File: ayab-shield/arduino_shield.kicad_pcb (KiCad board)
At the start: 2 copper layers, 73.1 x 53.3 mm, 35 parts, among them IC1 ULN2803A, IC2 ULN2803A, IC3 MCP2300X/P, IC4 MCP2300X/P, J1 Power, J2 Digital/PWM, J3 Analog, J4 Digital/PWM, X1 KLDX-0202-AC

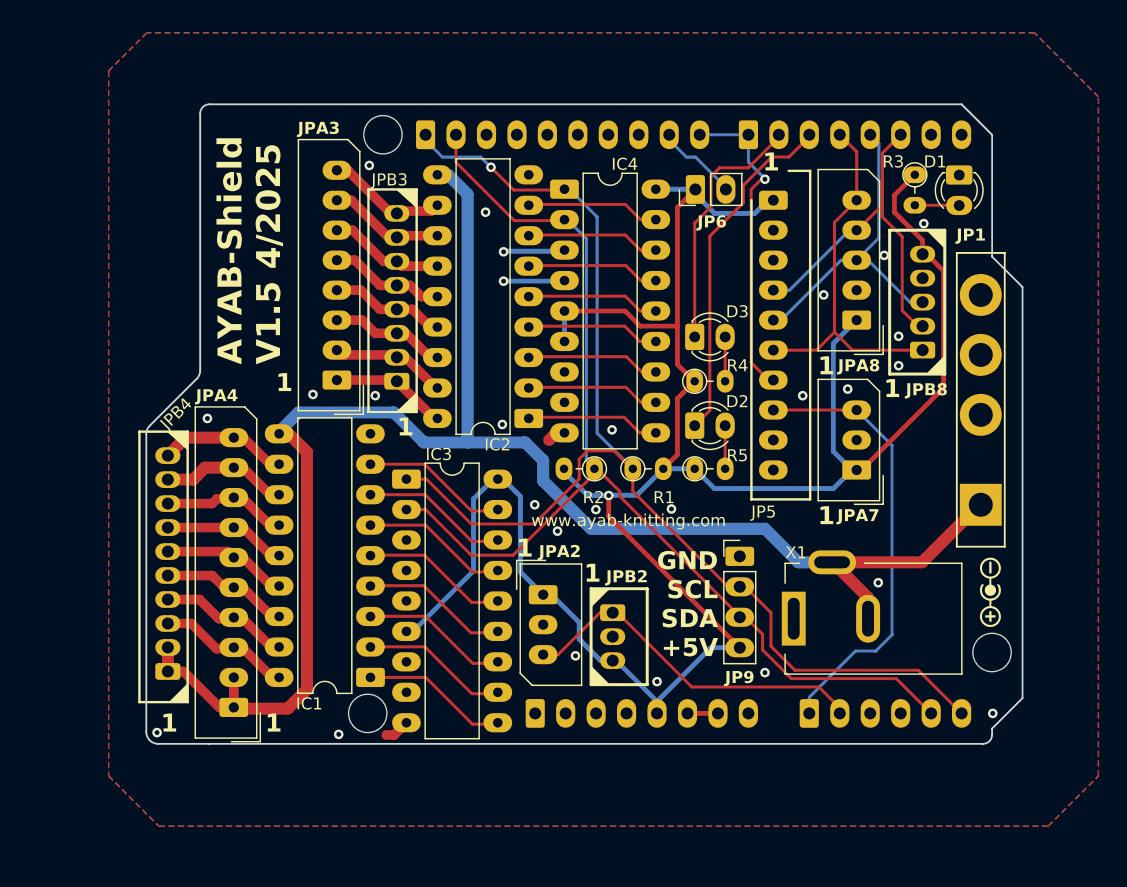
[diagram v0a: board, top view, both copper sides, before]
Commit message: Change footprints used on PCB to new footprints with '_LongPads' suffix
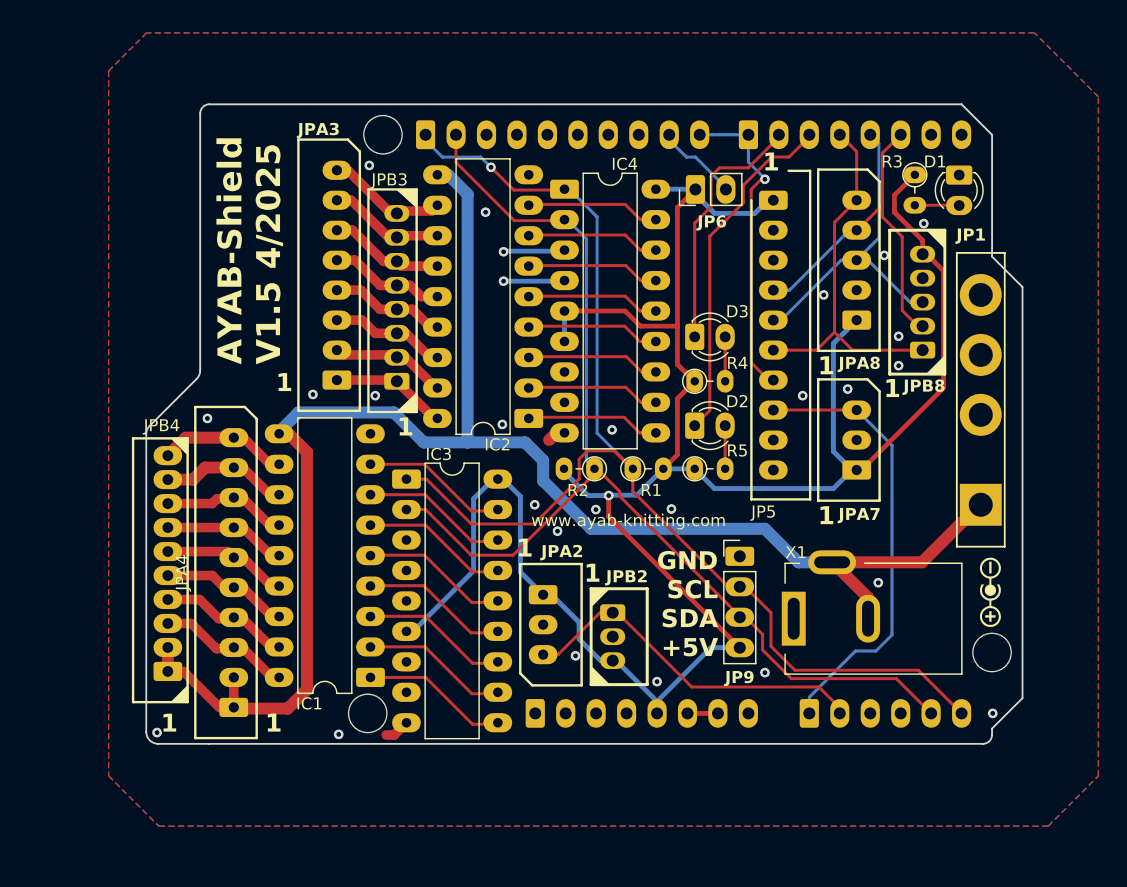
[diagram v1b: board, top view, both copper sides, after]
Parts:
- G***: value LOGO -> Polarity_Center_Negative_2mm_SilkScreen; footprint LOGO -> ayab-library:Polarity_Center_Negative_2mm_SilkScreen
- J2: footprint ayab-library:PinHeader_1x10_P2.54mm_Vertical -> ayab-library:PinHeader_1x10_P2.54mm_Vertical_LongPads
- JP5: footprint ayab-library:SHDR10W70P0X250_1X10_2740X490X590P -> ayab-library:SHDR10W70P0X250_1X10_2740X490X590P_LongPads
- JP6: footprint ayab-library:PinHeader_1x02_P2.54mm_Vertical -> ayab-library:PinHeader_1x02_P2.54mm_Vertical_LongPads
- JP9: footprint ayab-library:PinHeader_1x04_P2.54mm_Vertical -> ayab-library:PinHeader_1x04_P2.54mm_Vertical_LongPads
- JPA2, JPA7: footprint ayab-library:Molex_SPOX_5267-03A_1x03_P2.50mm_Vertical -> ayab-library:Molex_SPOX_5267-03A_1x03_P2.50mm_Vertical_LongPads
- JPA3: footprint ayab-library:Molex_SPOX_5267-08A_1x08_P2.50mm_Vertical -> ayab-library:Molex_SPOX_5267-08A_1x08_P2.50mm_Vertical_LongPads
- JPA4: footprint ayab-library:Molex_SPOX_5267-10A_1x10_P2.50mm_Vertical -> ayab-library:Molex_SPOX_5267-10A_1x10_P2.50mm_Vertical_LongPads
- JPA8: footprint ayab-library:Molex_SPOX_5267-05A_1x05_P2.50mm_Vertical -> ayab-library:Molex_SPOX_5267-05A_1x05_P2.50mm_Vertical_LongPads
- JPB4: footprint ayab-library:530141010 -> ayab-library:530141010_LongPads
- JPB8: footprint ayab-library:CONN-TH_A2004WV-5P -> ayab-library:CONN-TH_A2004WV-5P_LongPads
- R1, R2, R3, R4, R5: footprint ayab-library:R_Axial_DIN0204_L3.6mm_D1.6mm_P2.54mm_Vertical -> ayab-library:R_Axial_DIN0204_L3.6mm_D1.6mm_P2.54mm_Vertical_LongPads
- turned MH1 to -90 degrees

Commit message: Clean up
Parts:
- J1, J4: footprint ayab-library:PinHeader_1x08_P2.54mm_Vertical -> ayab-library:PinHeader_1x08_P2.54mm_Vertical_LongPads
- J3: footprint ayab-library:PinHeader_1x06_P2.54mm_Vertical -> ayab-library:PinHeader_1x06_P2.54mm_Vertical_LongPads
- JPB2: footprint ayab-library:CONN-TH_3P-P2.00_A2004WV-3P -> ayab-library:530140310_LongPads
- JPB3: footprint ayab-library:530140810 -> ayab-library:530140810_LongPads
- JPB8: footprint ayab-library:CONN-TH_A2004WV-5P_LongPads -> ayab-library:530140510_LongPads
- moved JPB8 4.04 mm to (175.0, 97.2)
- moved JPB2 2.04 mm to (149.1, 119.1)
- moved JPA3 0.46 mm to (125.6, 99.7)

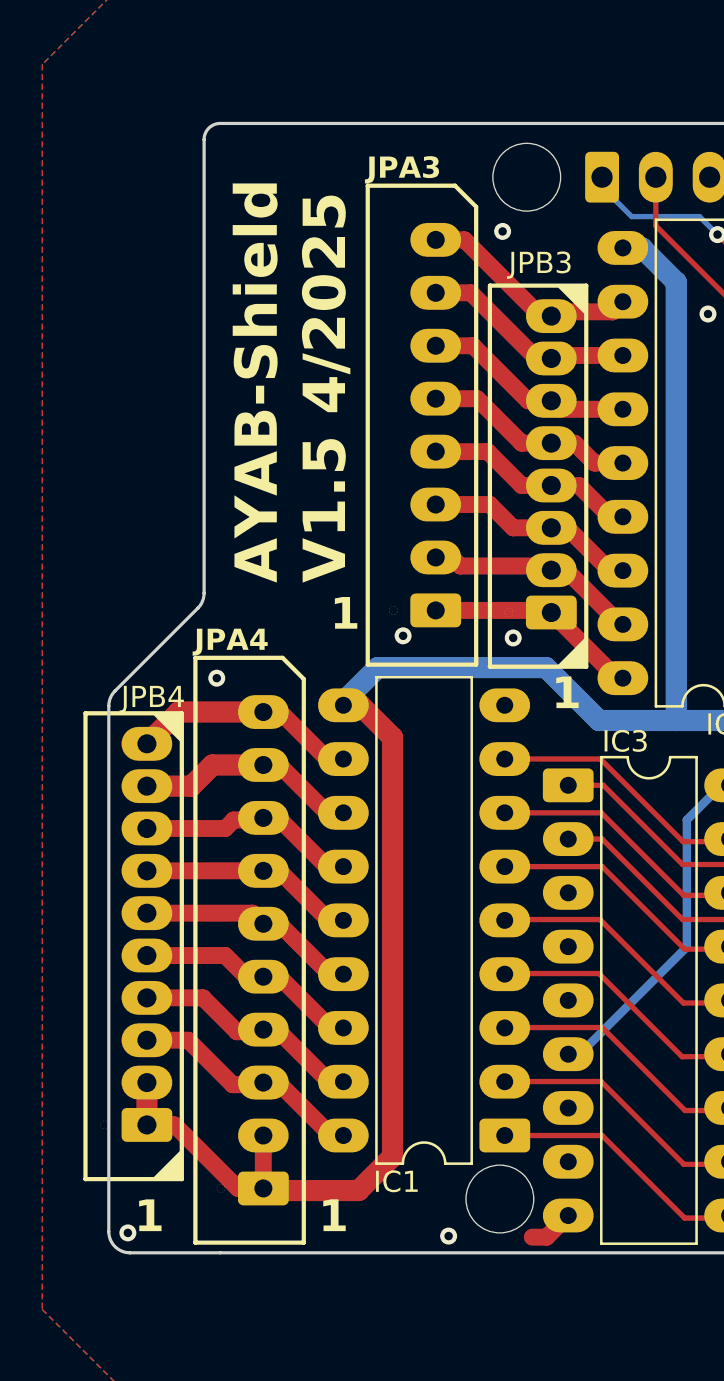
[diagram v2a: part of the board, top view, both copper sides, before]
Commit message: Reverse orientation of solenoid headers and extend PCB by 1mm
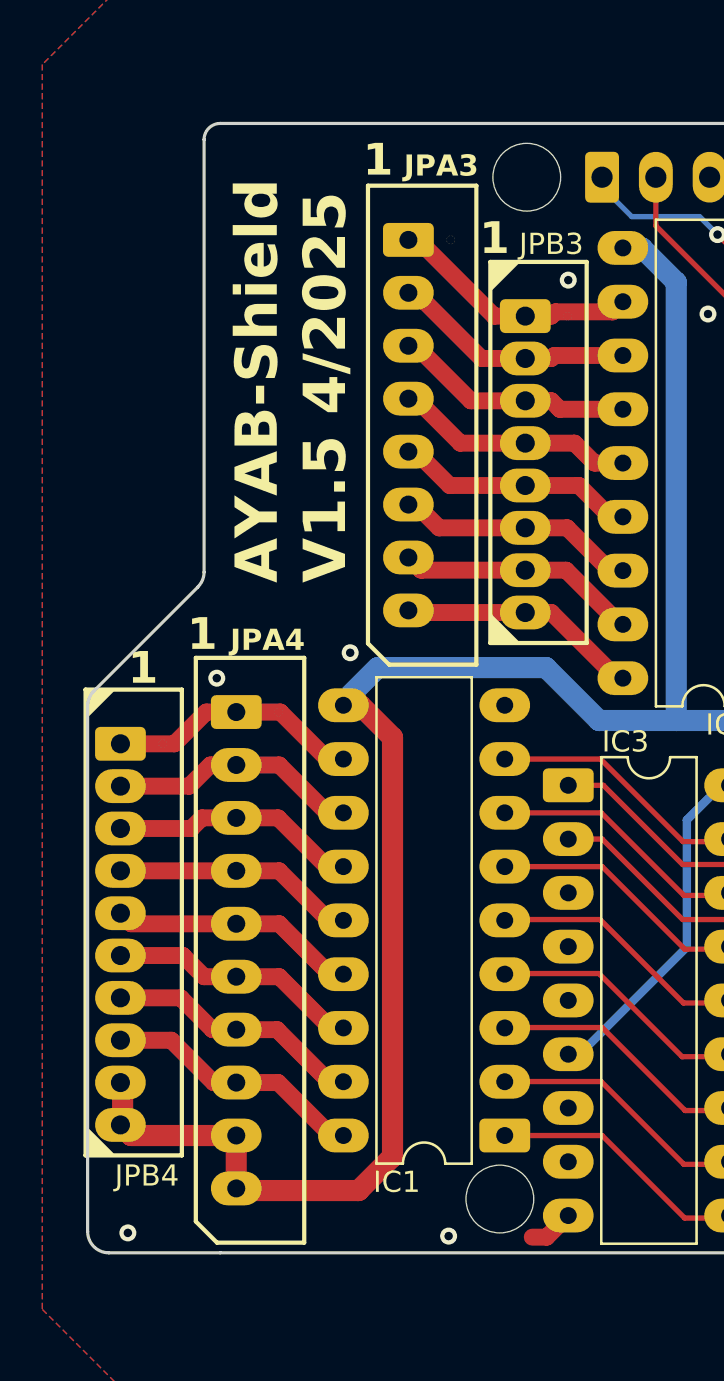
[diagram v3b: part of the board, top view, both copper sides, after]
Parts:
- moved JPA4 22.5 mm to (116.2, 104.5), turned to -90 degrees
- moved JPB4 18.0 mm to (110.8, 106.0), turned to 90 degrees
- moved JPA3 17.5 mm to (124.3, 82.2), turned to -90 degrees
- moved JPB3 14.1 mm to (129.9, 85.8), turned to 90 degrees
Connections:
- JPA3 pad 1: Net-(IC2-O1) -> Net-(IC2-O8)
- JPA3 pad 2: Net-(IC2-O2) -> Net-(IC2-O7)
- JPA3 pad 3: Net-(IC2-O3) -> Net-(IC2-O6)
- JPA3 pad 4: Net-(IC2-O4) -> Net-(IC2-O5)
- JPA3 pad 5: Net-(IC2-O5) -> Net-(IC2-O4)
- JPA3 pad 6: Net-(IC2-O6) -> Net-(IC2-O3)
- JPA3 pad 7: Net-(IC2-O7) -> Net-(IC2-O2)
- JPA3 pad 8: Net-(IC2-O8) -> Net-(IC2-O1)
- JPA4 pad 1: +15V -> Net-(IC1-O8)
- JPA4 pad 10: Net-(IC1-O8) -> +15V
- JPA4 pad 2: +15V -> Net-(IC1-O7)
- JPA4 pad 3: Net-(IC1-O1) -> Net-(IC1-O6)
- JPA4 pad 4: Net-(IC1-O2) -> Net-(IC1-O5)
- JPA4 pad 5: Net-(IC1-O3) -> Net-(IC1-O4)
- JPA4 pad 6: Net-(IC1-O4) -> Net-(IC1-O3)
- JPA4 pad 7: Net-(IC1-O5) -> Net-(IC1-O2)
- JPA4 pad 8: Net-(IC1-O6) -> Net-(IC1-O1)
- JPA4 pad 9: Net-(IC1-O7) -> +15V
- JPB3 pad 1: Net-(IC2-O1) -> Net-(IC2-O8)
- JPB3 pad 2: Net-(IC2-O2) -> Net-(IC2-O7)
- JPB3 pad 3: Net-(IC2-O3) -> Net-(IC2-O6)
- JPB3 pad 4: Net-(IC2-O4) -> Net-(IC2-O5)
- JPB3 pad 5: Net-(IC2-O5) -> Net-(IC2-O4)
- JPB3 pad 6: Net-(IC2-O6) -> Net-(IC2-O3)
- JPB3 pad 7: Net-(IC2-O7) -> Net-(IC2-O2)
- JPB3 pad 8: Net-(IC2-O8) -> Net-(IC2-O1)
- JPB4 pad 1: +15V -> Net-(IC1-O8)
- JPB4 pad 10: Net-(IC1-O8) -> +15V
- JPB4 pad 2: +15V -> Net-(IC1-O7)
- JPB4 pad 3: Net-(IC1-O1) -> Net-(IC1-O6)
- JPB4 pad 4: Net-(IC1-O2) -> Net-(IC1-O5)
- JPB4 pad 5: Net-(IC1-O3) -> Net-(IC1-O4)
- JPB4 pad 6: Net-(IC1-O4) -> Net-(IC1-O3)
- JPB4 pad 7: Net-(IC1-O5) -> Net-(IC1-O2)
- JPB4 pad 8: Net-(IC1-O6) -> Net-(IC1-O1)
- JPB4 pad 9: Net-(IC1-O7) -> +15V
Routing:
- net Net-(IC1-O6): track 10.1 -> 11.7 mm
- net Net-(IC1-O3): track 10.4 -> 11.9 mm
- net Net-(IC1-O4): track 10.2 -> 11.7 mm
- net Net-(IC1-O2): track 10.6 -> 12.2 mm
- net Net-(IC1-O5): track 9.95 -> 11.5 mm
- net Net-(IC1-O1): track 10.8 -> 12.4 mm
- net Net-(IC2-O8): track 10.5 -> 12.0 mm
- net Net-(IC2-O3): track 10.0 -> 11.4 mm
- net Net-(IC2-O7): track 10.1 -> 11.5 mm
- net Net-(IC2-O6): track 9.98 -> 11.4 mm
- net Net-(IC2-O5): track 9.99 -> 11.4 mm
- net Net-(IC2-O4): track 10.0 -> 11.4 mm
- net Net-(IC2-O1): track 10.5 -> 11.9 mm
- net Net-(IC2-O2): track 10.0 -> 11.4 mm
- net Net-(IC1-O7): track 10.6 -> 11.9 mm
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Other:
- board size 73.1 x 53.3 mm -> 74.1 x 53.3 mm

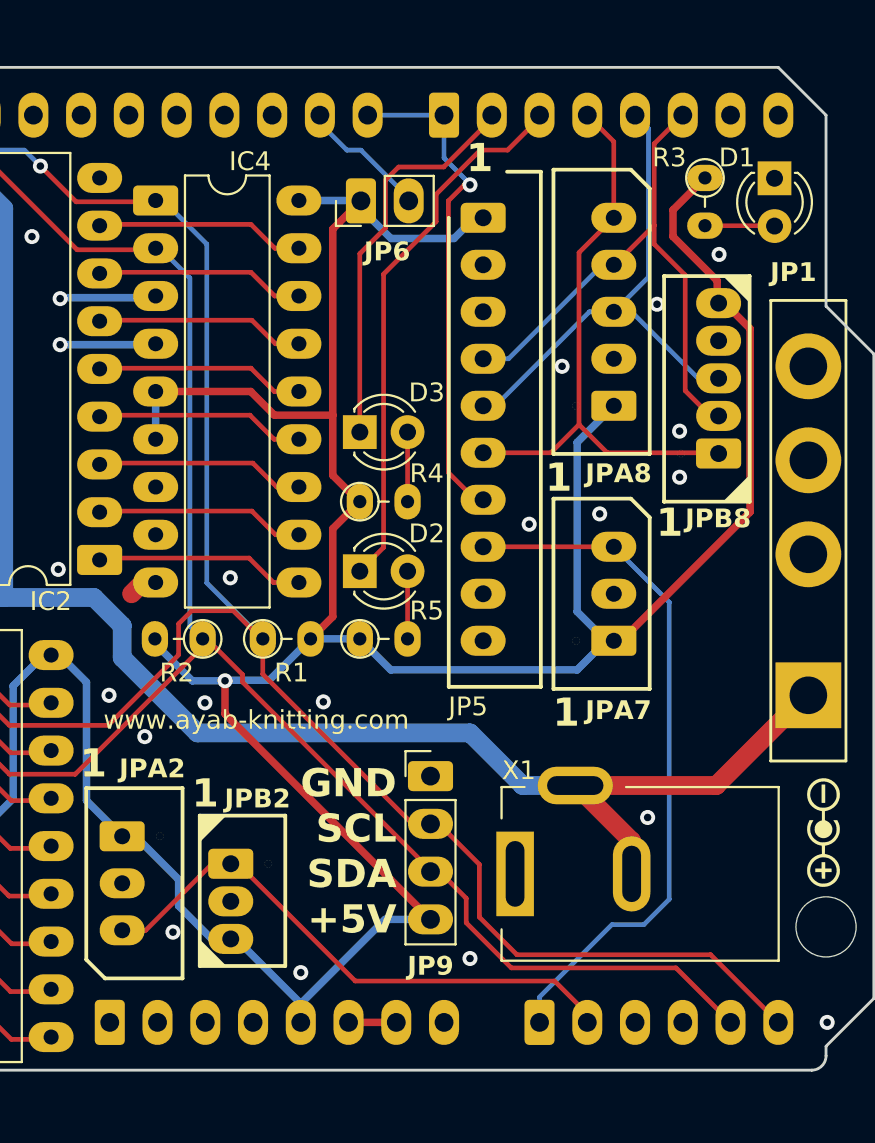
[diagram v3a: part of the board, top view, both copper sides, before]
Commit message: Re-orient JPA7, JPA8, and JPB8
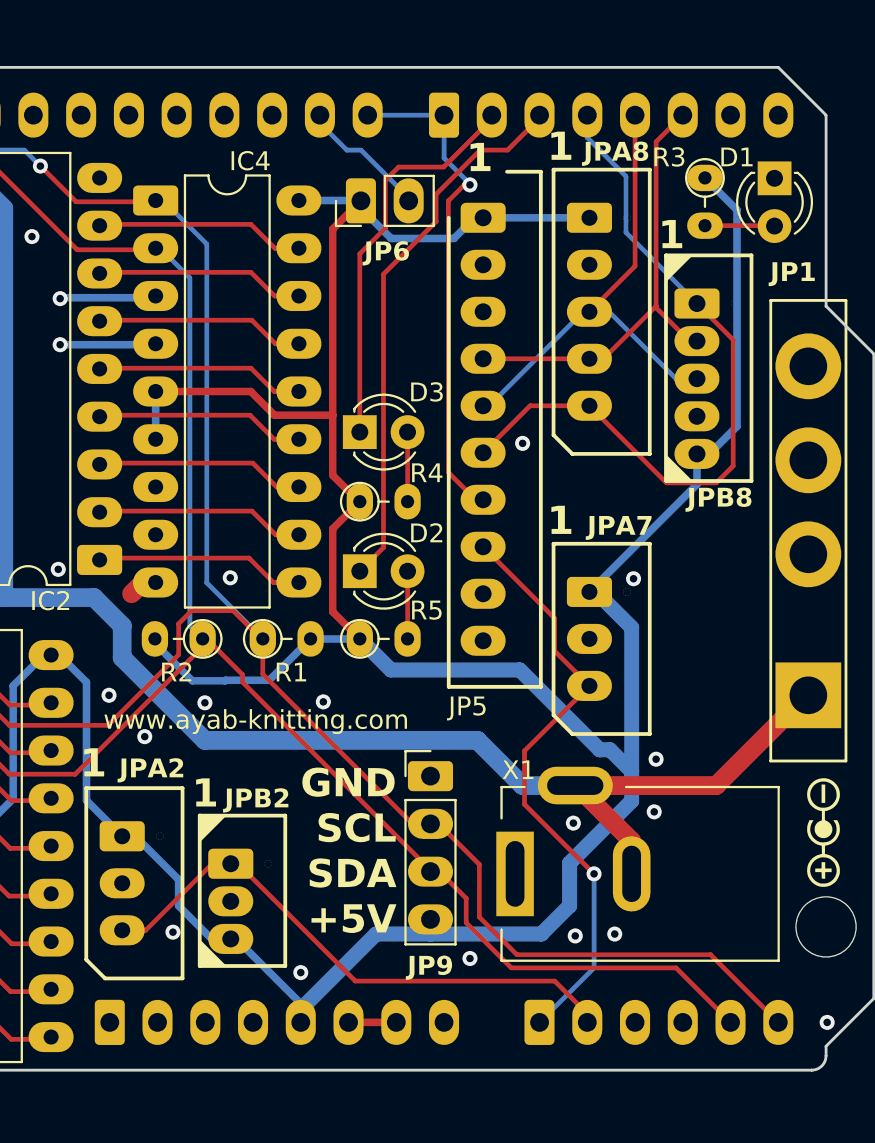
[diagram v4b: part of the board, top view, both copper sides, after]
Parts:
- moved JPA8 10.1 mm to (168.2, 84.7), turned to -90 degrees
- moved JPB8 8.06 mm to (173.9, 89.3), turned to 90 degrees
- moved JPA7 2.90 mm to (168.2, 104.6), turned to -90 degrees
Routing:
- net /ENC_C: track 31.8 -> 38.6 mm
- net /ENC_A: track 30.3 -> 24.1 mm
- net /EOL_R: track 37.3 -> 31.8 mm, vias 0 -> 1
- net +5V: track 193.4 -> 192.1 mm, vias 1 -> 0
- net /ENC_B: track 27.8 -> 26.7 mm
- net GND: track 17.5 -> 16.6 mm, vias 26 -> 25
